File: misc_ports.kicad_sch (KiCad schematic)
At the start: 25 parts

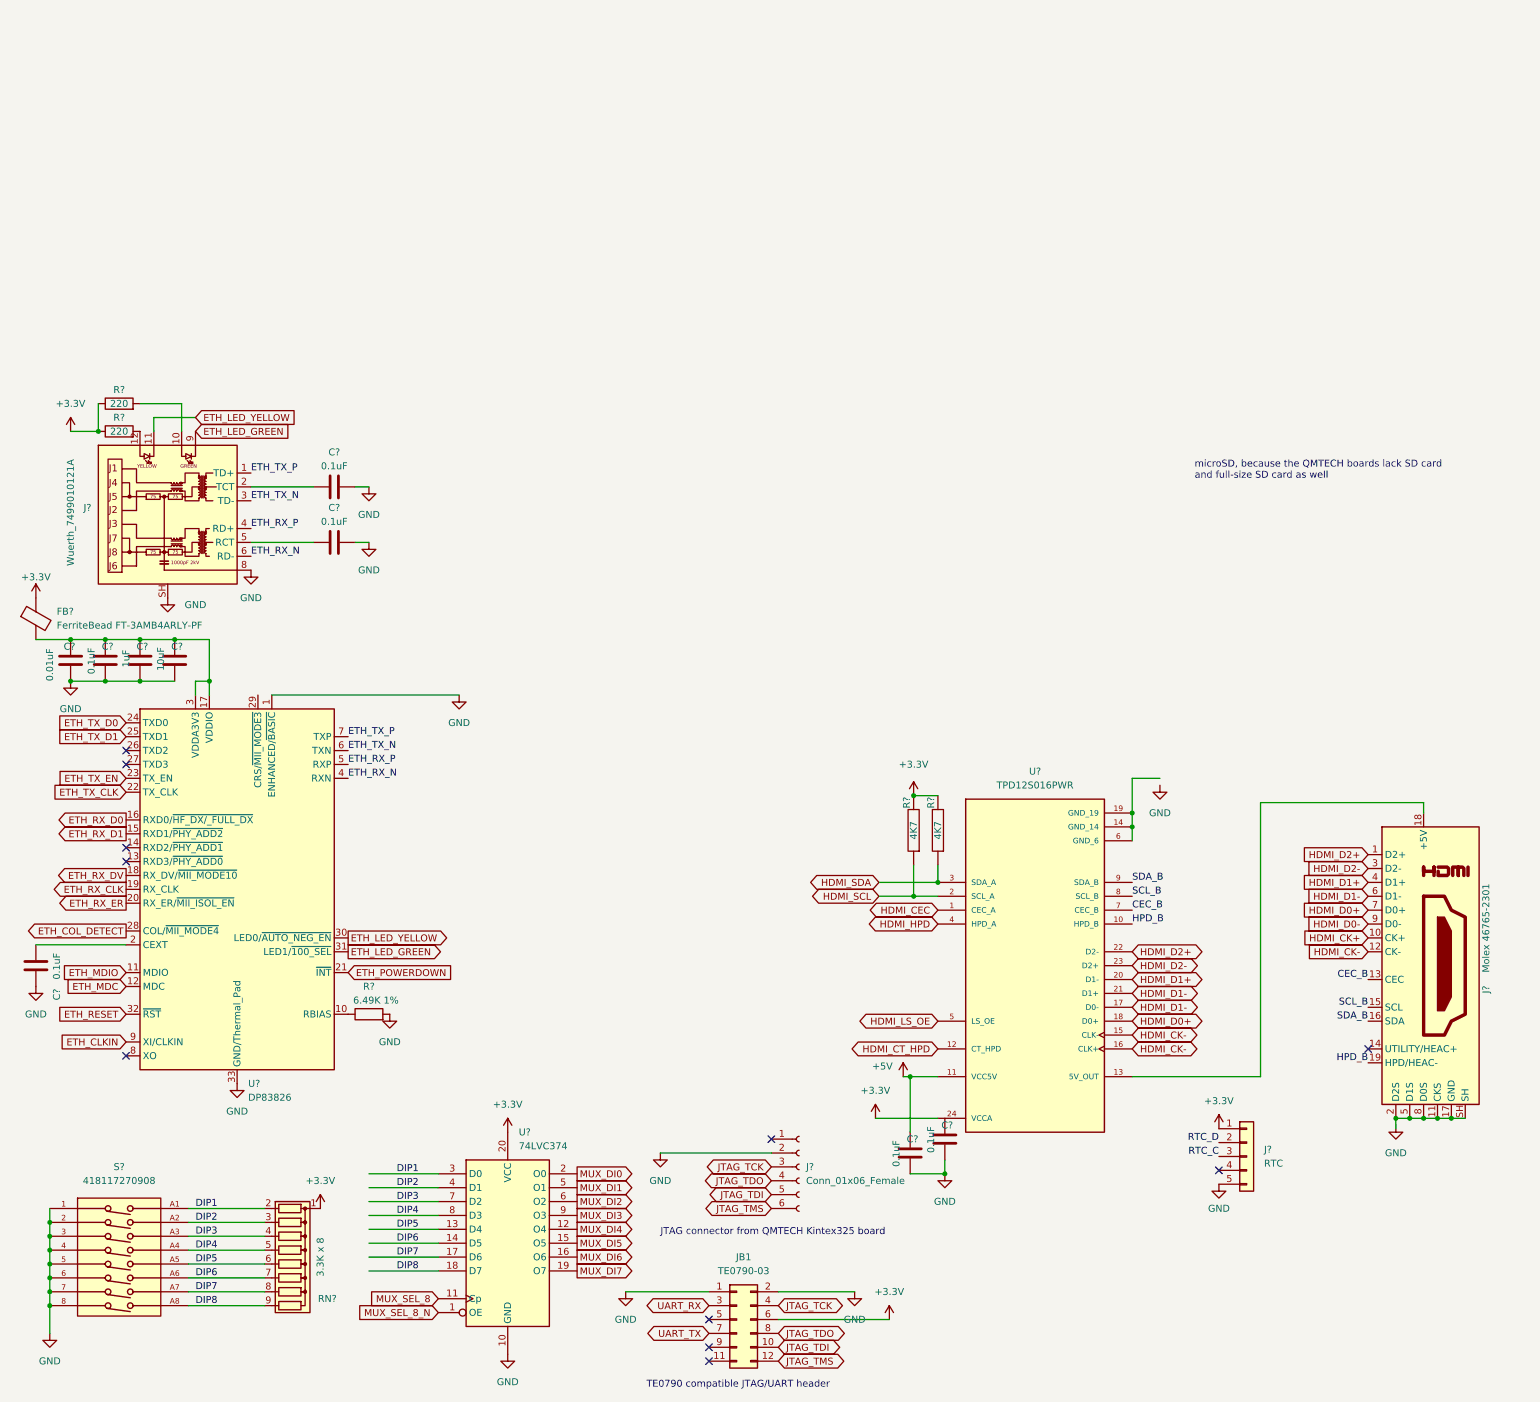
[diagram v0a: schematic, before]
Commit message: add microSD and full-sized SD card slots
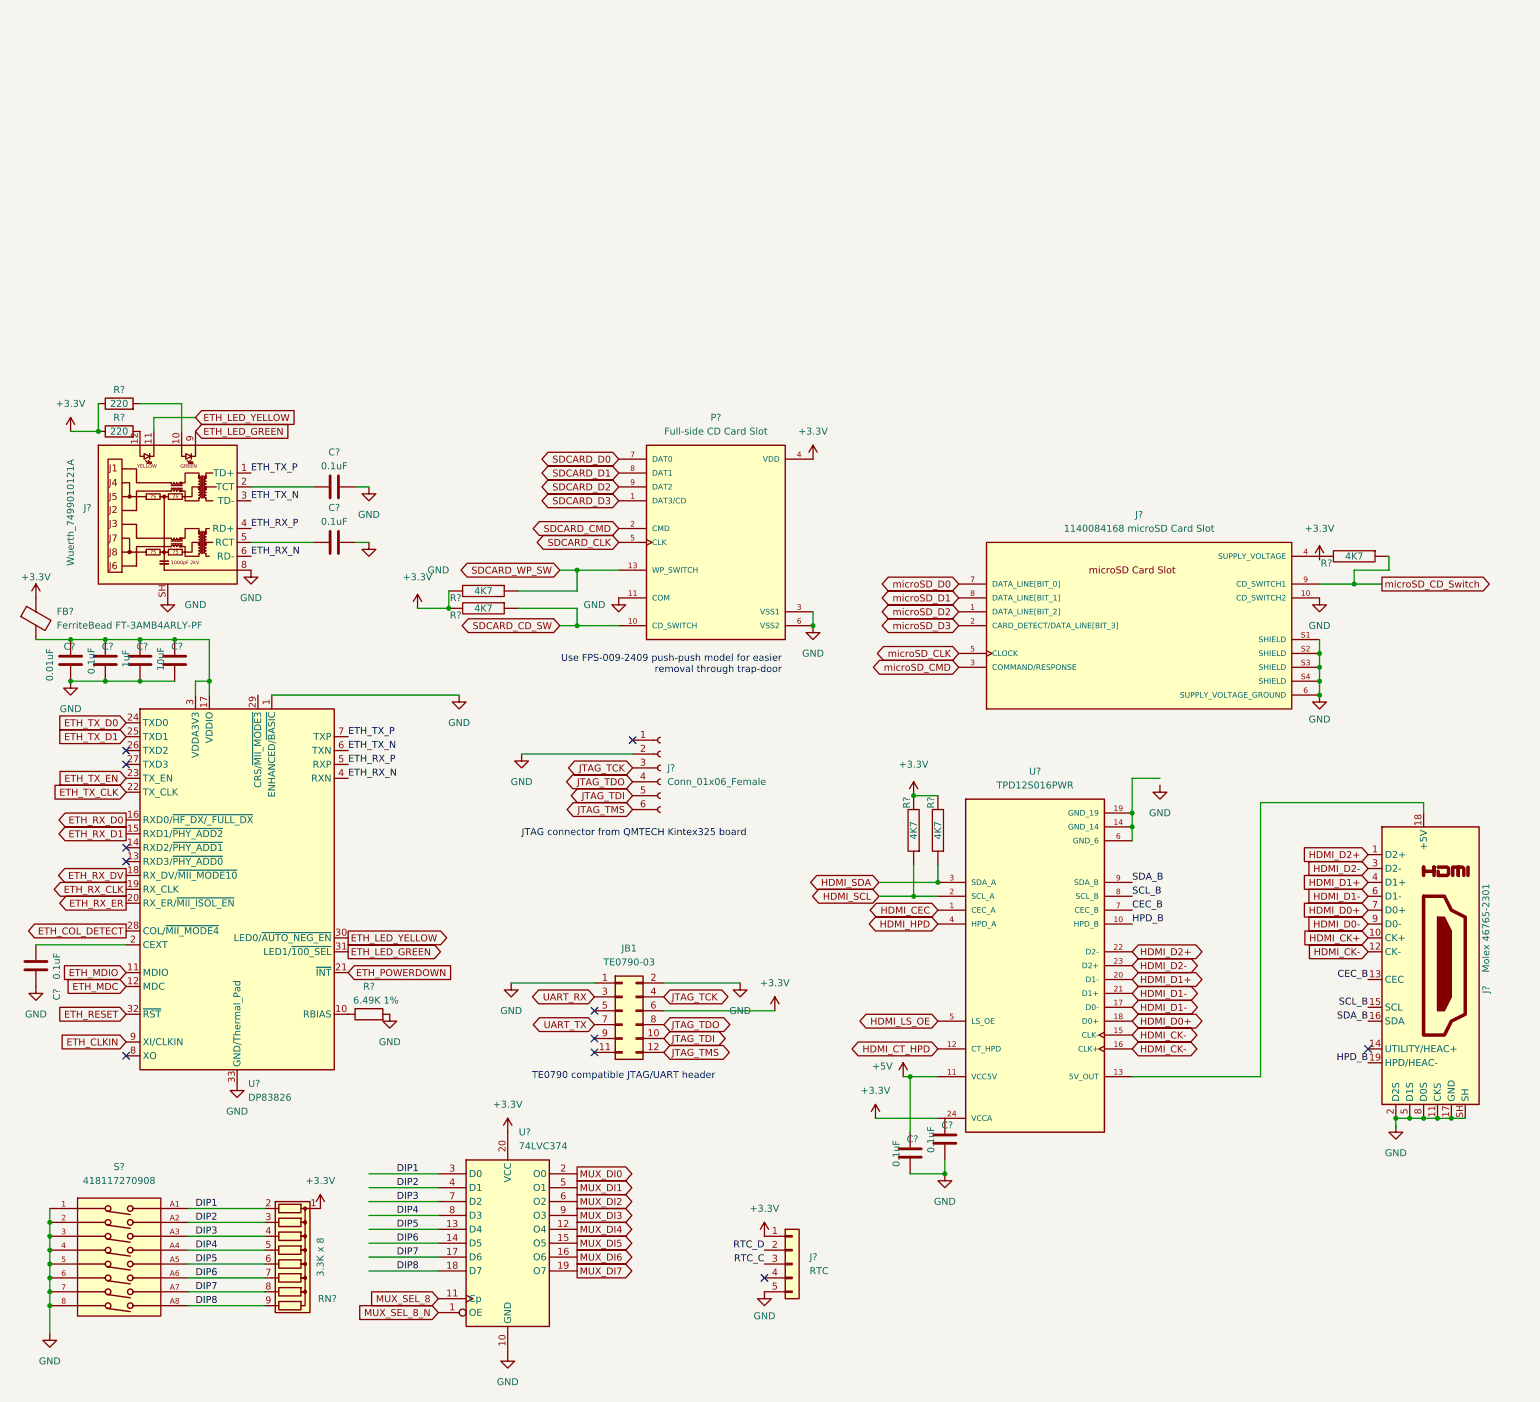
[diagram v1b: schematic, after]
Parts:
- added J?: 1140084168 microSD Card Slot, AMPHENOL_1140084168, symbol 00Project-microSD:1140084168 microSD Card Slot
- added P?: Full-side CD Card Slot, YAMAICHI_FPS009-2405-0, symbol 00Project-SDcard:FPS009-2405-0
- added R? (x3): 4K7, Resistor_THT:R_Box_L8.4mm_W2.5mm_P5.08mm, symbol pspice:R
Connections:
- net +3V3: now also P?.4 (VDD), R?.2, R?.2
- net GND: now also J?.10 (CD_SWITCH2), J?.6 (SUPPLY_VOLTAGE_GROUND), J?.S1 (SHIELD), J?.S2 (SHIELD), J?.S3 (SHIELD), J?.S4 (SHIELD), P?.11 (COM), P?.3 (VSS1), P?.6 (VSS2)
- new net: J?.4 (SUPPLY_VOLTAGE), R?.2
- new net SDCARD_CD_SW: P?.10 (CD_SWITCH), R?.1
- new net SDCARD_CLK: P?.5 (CLK)
- new net SDCARD_CMD: P?.2 (CMD)
- new net SDCARD_D0: P?.7 (DAT0)
- new net SDCARD_D1: P?.8 (DAT1)
- new net SDCARD_D2: P?.9 (DAT2)
- new net SDCARD_D3: P?.1 (DAT3/CD)
- new net SDCARD_WP_SW: P?.13 (WP_SWITCH), R?.1
- new net microSD_CD_Switch: J?.9 (CD_SWITCH1), R?.1
- new net microSD_CLK: J?.5 (CLOCK)
- new net microSD_CMD: J?.3 (COMMAND/RESPONSE)
- new net microSD_D0: J?.7 (DATA_LINE[BIT_0])
- new net microSD_D1: J?.8 (DATA_LINE[BIT_1])
- new net microSD_D2: J?.1 (DATA_LINE[BIT_2])
- new net microSD_D3: J?.2 (CARD_DETECT/DATA_LINE[BIT_3])
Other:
- note added: "Use FPS-009-2409 push-push model for easier removal through trap-door"
- note removed: "microSD, because the QMTECH boards lack SD card and full-size SD card as well"
- moved on the sheet: J?, JB1

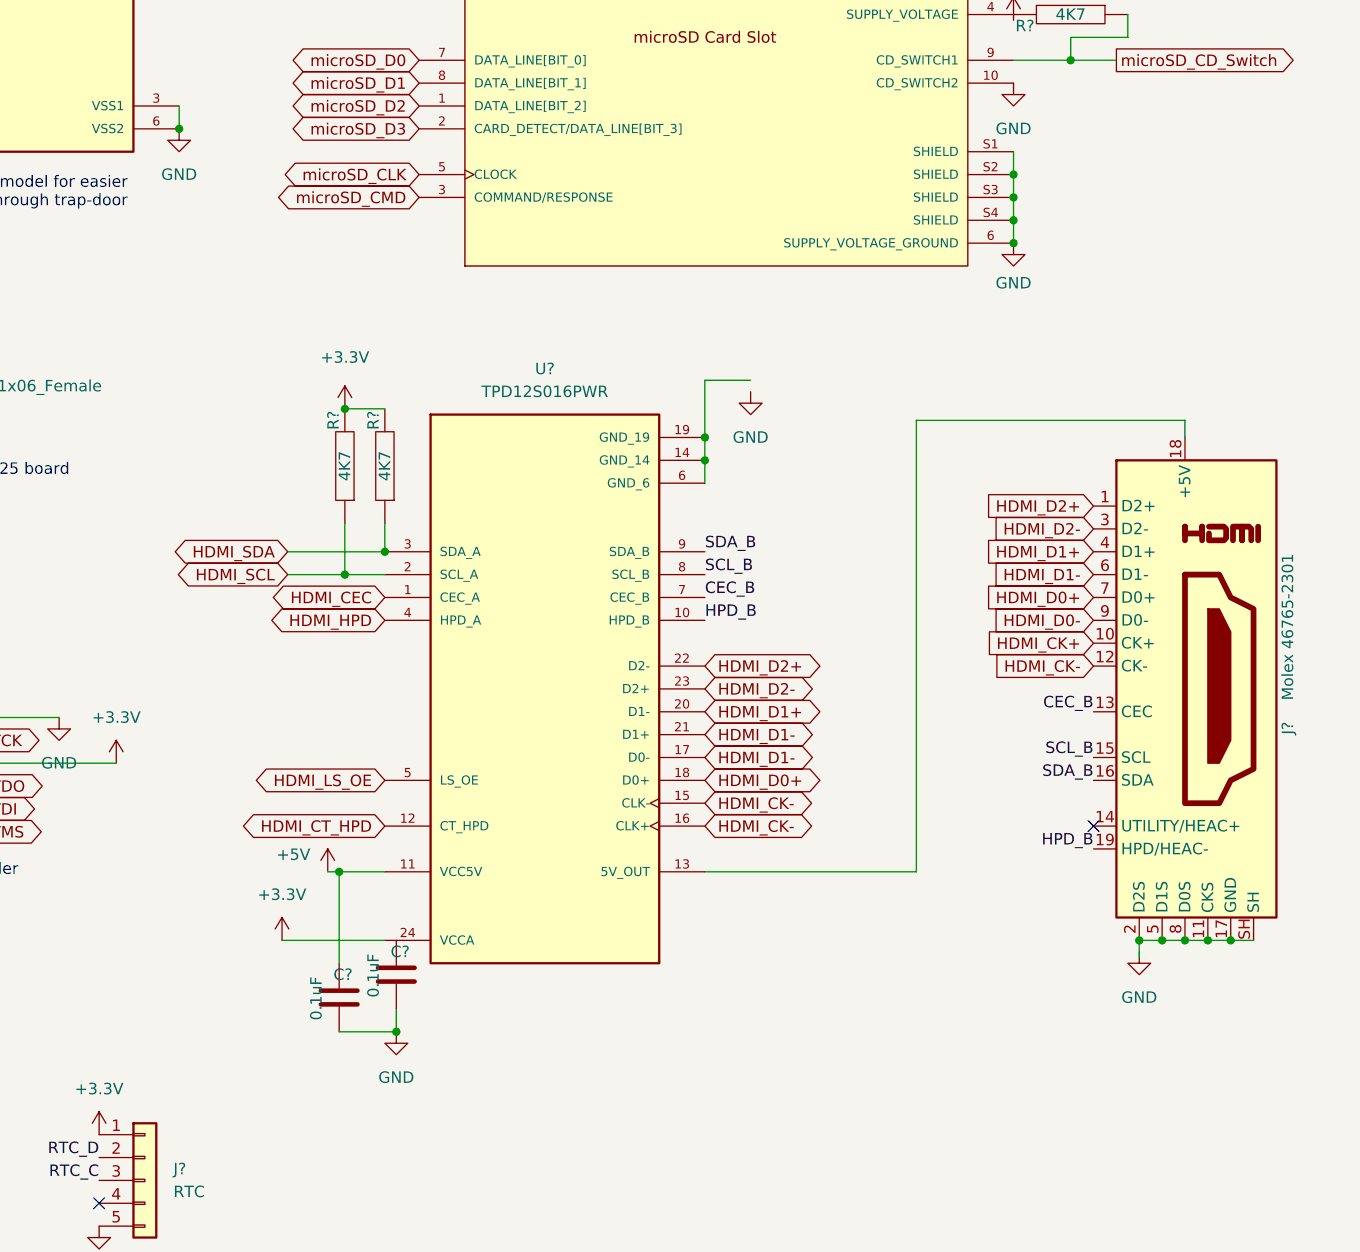
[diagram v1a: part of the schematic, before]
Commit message: switch to same HDMI helper chip as on MEGA65 R4 PCB
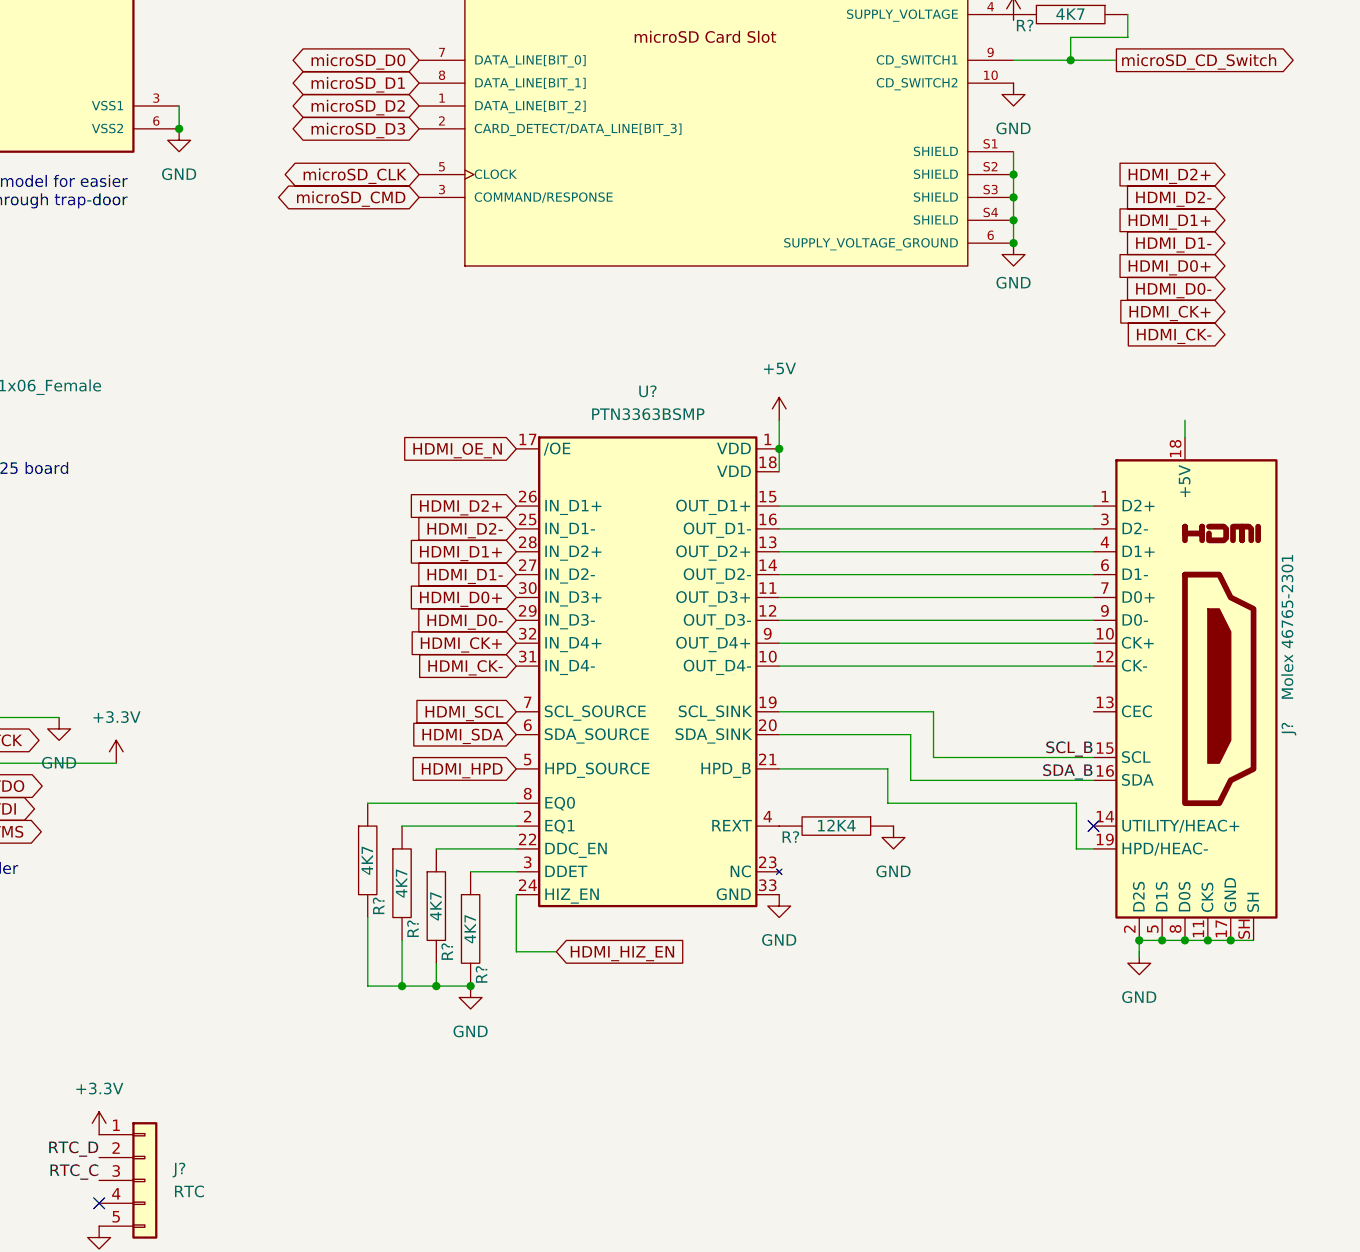
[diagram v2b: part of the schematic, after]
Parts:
- removed C? (x2): 0.1uF, symbol Device:C
- removed R? (x2): 4K7, Resistor_THT:R_Box_L8.4mm_W2.5mm_P5.08mm, symbol pspice:R
- removed U?: TPD12S016PWR, SOP65P640X120-24N, symbol 00Project-HDMI-Helper:TPD12S016PWR
- added R? (x4): 4K7, Resistor_THT:R_Box_L8.4mm_W2.5mm_P5.08mm, symbol pspice:R
- added R?: 12K4, Resistor_THT:R_Box_L8.4mm_W2.5mm_P5.08mm, symbol pspice:R
- added U?: PTN3363BSMP, snapeda:QFN50P500X500X85-33N, symbol 00Project-HDMI-Helper:PTN3363BSMP
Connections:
- net +5V: now also U?.1 (VDD), U?.18 (VDD)
- net GND: now also R?.1, R?.2, R?.2, R?.2, R?.2, U?.33 (GND)
- net HDMI_CK+: now also U?.32 (IN_D4+); no longer J?.10 (CK+)
- net HDMI_CK-: now also U?.31 (IN_D4-); no longer J?.12 (CK-)
- net HDMI_D0+: now also U?.30 (IN_D3+); no longer J?.7 (D0+)
- net HDMI_D0-: now also U?.29 (IN_D3-); no longer J?.9 (D0-)
- net HDMI_D1+: now also U?.28 (IN_D2+); no longer J?.4 (D1+)
- net HDMI_D1-: now also U?.27 (IN_D2-); no longer J?.6 (D1-)
- net HDMI_D2+: now also U?.26 (IN_D1+); no longer J?.1 (D2+)
- net HDMI_D2-: now also U?.25 (IN_D1-); no longer J?.3 (D2-)
- net HDMI_HPD: now also U?.5 (HPD_SOURCE)
- net HDMI_SCL: now also U?.7 (SCL_SOURCE)
- net HDMI_SDA: now also U?.6 (SDA_SOURCE)
- net SCL_B: now also U?.19 (SCL_SINK)
- net SDA_B: now also U?.20 (SDA_SINK)
- net CEC_B: no longer names the net of J?.13 (CEC)
- net HPD_B: no longer names the net of J?.19 (HPD/HEAC-)
- net HPD_B: now also U?.21 (HPD_B)
- new net: R?.1, U?.2 (EQ1)
- new net: R?.1, U?.22 (DDC_EN)
- new net: R?.1, U?.3 (DDET)
- new net: R?.1, U?.8 (EQ0)
- new net: J?.1 (D2+), U?.15 (OUT_D1+)
- new net: J?.10 (CK+), U?.9 (OUT_D4+)
- new net: J?.12 (CK-), U?.10 (OUT_D4-)
- new net: J?.3 (D2-), U?.16 (OUT_D1-)
- new net: J?.4 (D1+), U?.13 (OUT_D2+)
- new net: J?.6 (D1-), U?.14 (OUT_D2-)
- new net: J?.7 (D0+), U?.11 (OUT_D3+)
- new net: J?.9 (D0-), U?.12 (OUT_D3-)
- new net: R?.2, U?.4 (REXT)
- new net HDMI_HIZ_EN: U?.24 (HIZ_EN)
- new net HDMI_OE_N: U?.17 (/OE)
